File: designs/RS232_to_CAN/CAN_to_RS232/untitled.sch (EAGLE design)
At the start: 22 parts, among them IC1 UART_RS232, IC2 STM32F042K6T6TR, IC3 CAN_Receiver, J1 Programmer, J2 CAN, J3 RS232

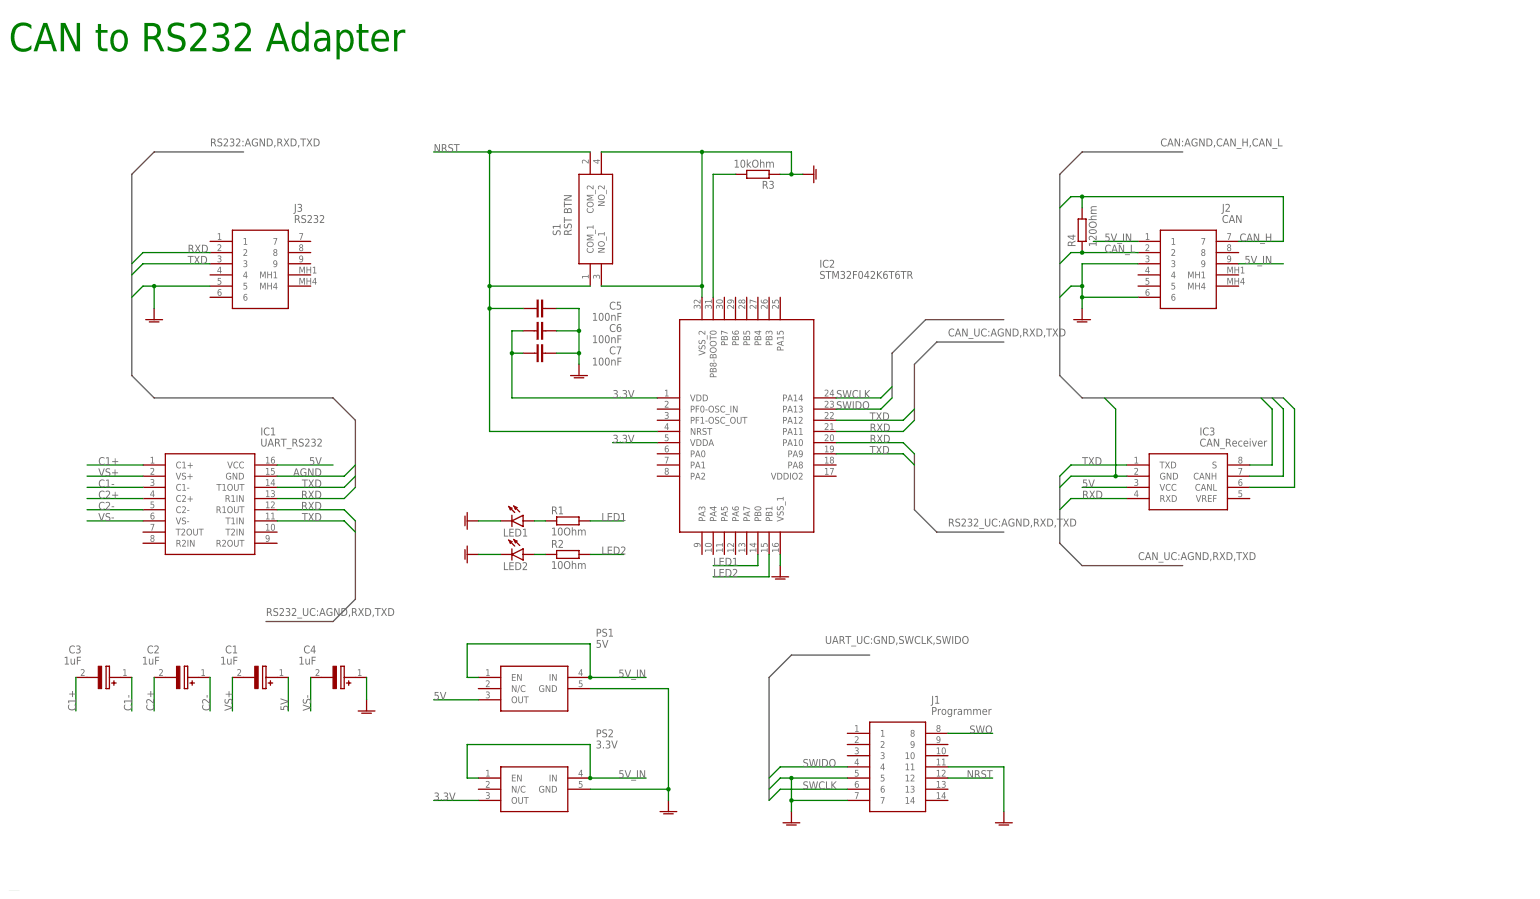
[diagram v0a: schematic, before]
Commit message: ESP32 brd layout
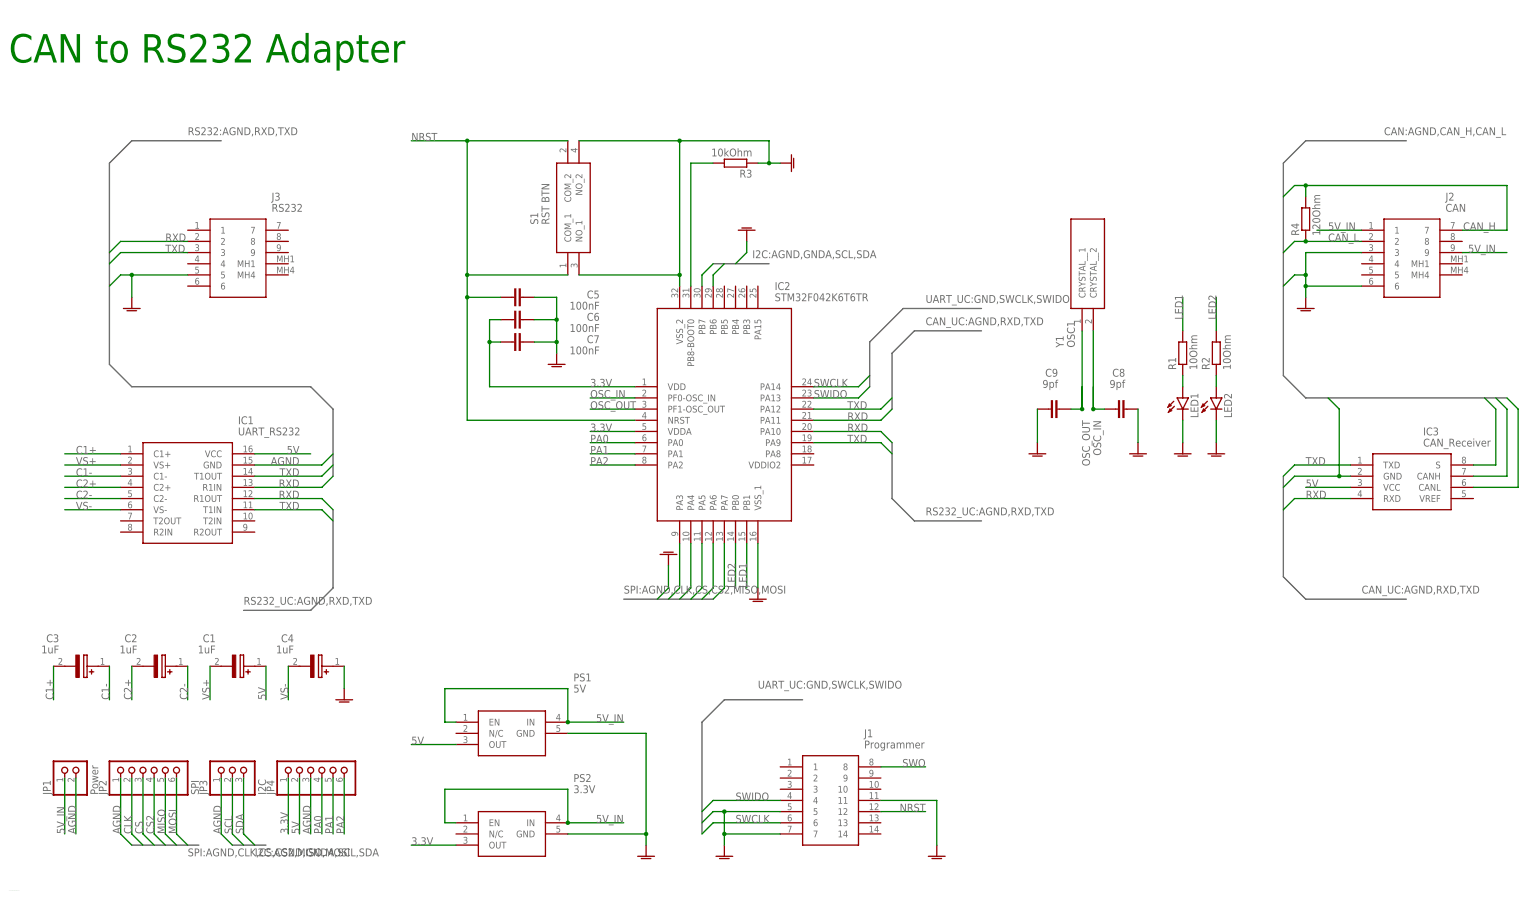
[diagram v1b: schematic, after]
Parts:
- added C8, C9: 9pf, CommonParts:C-EU_805C0805
- added JP1: Power, pinhead:PINHD-1X2/90
- added JP2: SPI, pinhead:PINHD-1X6/90
- added JP3: I2C, pinhead:PINHD-1X3/90
- added JP4: (no value), pinhead:PINHD-1X6/90
- added Y1: OSC1, MouserUseful:CM7V-T1A-32.768KHZ-7PF-100PPM-
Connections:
- removed net N$4: IC2.PB1
- removed net N$5: C2.+
- removed net N$6: C2.-
- removed net N$7: C3.+
- removed net N$8: IC2.PB0
- new net CLK: IC2.PA5, JP2.2
- new net CS: IC2.PA4, JP2.3
- new net CS2: IC2.PA3, JP2.4
- new net MISO: IC2.PA6, JP2.5
- new net MOSI: IC2.PA7, JP2.6
- new net OSC_IN: C8.1, IC2.PF0-OSC_IN, Y1.CRYSTAL__2
- new net OSC_OUT: C9.2, IC2.PF1-OSC_OUT, Y1.CRYSTAL__1
- new net PA0: IC2.PA0, JP4.4
- new net PA1: IC2.PA1, JP4.5
- new net PA2: IC2.PA2, JP4.6
- new net SCL: IC2.PB6, JP3.2
- new net SDA: IC2.PB7, JP3.3
- net 3.3V: now also JP4.1
- net 5V: now also JP4.2
- net 5V_IN: now also JP1.1
- net AGND: now also JP1.2, JP2.1, JP3.1, JP4.3
- net C1-: now also C3.+
- net C2+: now also C2.-
- net C2-: now also C2.+
- net GNDA: now also C8.2, C9.1
- net LED1: now also IC2.PB1
- net LED2: now also IC2.PB0
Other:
- moved on the sheet: C1, C2, C3, C4, C5, C6, C7, IC1, IC2, IC3, J1, J2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

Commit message: added brd layout for RS232 to can
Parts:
- J1: value Programmer -> RS232; device MouserUseful:FTSH-107-01-L-DV-K-A -> MouserUseful:K202XHT-E9S-N
- J2: value CAN -> Programmer; device MouserUseful:K202XHT-E9S-N -> MouserUseful:FTSH-107-01-L-DV-K-A
- J3: value RS232 -> CAN
- JP1: value Power -> (none); device pinhead:PINHD-1X2/90 -> pinhead:PINHD-1X2
- JP2: value SPI -> (none); device pinhead:PINHD-1X6/90 -> pinhead:PINHD-1X6
- JP3: value I2C -> (none); device pinhead:PINHD-1X3/90 -> pinhead:PINHD-1X3
- JP4: device pinhead:PINHD-1X6/90 -> pinhead:PINHD-1X6
- R1: value 10Ohm -> 10kOhm
- R3: value 10kOhm -> 10Ohm
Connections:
- removed net AGND: IC1.GND, IC3.GND, IC3.S, J2.3, J2.6, J3.5, JP1.2, JP2.1, JP3.1, JP4.3
- removed net CAN_H: IC3.CANH, J2.7, R4.2
- removed net CAN_L: IC3.CANL, J2.2, R4.1
- removed net GNDA: C4.+, C5.2, C6.2, C7.2, C8.2, C9.1, IC2.VSS_1, IC2.VSS_2, J1.11, LED1.C, LED2.C, PS1.GND, PS2.GND, R3.1, S1.NO_1, S1.NO_2
- new net CAN_N: IC3.CANL, J3.2, R4.1
- new net CAN_P: IC3.CANH, J3.7, R4.2
- new net CAN_UC_XD_N: IC2.PA11, IC3.RXD
- new net CAN_UC_XD_P: IC2.PA12, IC3.TXD
- new net RXD_UC: IC1.R1OUT, IC2.PA10
- new net TXD_UC: IC1.T1IN, IC2.PA9
- net 3.3V: now also J2.3
- net 5V: now also C3.+; no longer C1.+
- net 5V_IN: now also J3.1, J3.9; no longer J2.1, J2.9
- net C1+: now also C1.-; no longer C3.-
- net C1-: now also C1.+; no longer C3.+
- net CLK: now also JP2.4; no longer JP2.2
- net CS: now also JP2.5; no longer JP2.3
- net CS2: now also JP2.6; no longer JP2.4
- net GND: now also C4.+, C5.2, C6.2, C7.2, C8.1, C9.2, IC1.GND, IC2.VSS_1, IC2.VSS_2, IC3.GND, IC3.S, J2.11, J2.5, J2.7, J3.3, J3.6, JP1.2, JP2.1, JP3.1, JP4.3, LED1.C, LED2.C, PS1.GND, PS2.GND, R1.1, S1.NO_1, S1.NO_2; no longer J1.7
- net LED1: now also R2.2; no longer R1.2
- net LED2: now also R3.2; no longer R2.2
- net MISO: now also JP2.3; no longer JP2.5
- net MOSI: now also JP2.2; no longer JP2.6
- net N$1: now also R2.1; no longer R1.1
- net N$2: now also R3.1; no longer R2.1
- net N$3: now also R1.2; no longer R3.2
- net NRST: now also J2.12; no longer J1.12
- net OSC_IN: now also C9.1; no longer C8.1
- net OSC_OUT: now also C8.2; no longer C9.2
- net RXD: now also J1.2; no longer IC1.R1OUT, IC2.PA10, IC2.PA11, IC3.RXD, J3.2
- net SWCLK: now also J2.6; no longer J1.6
- net SWIDO: now also J2.4; no longer J1.4
- net SWO: now also J2.8; no longer J1.8
- net TXD: now also J1.3; no longer IC1.T1IN, IC2.PA12, IC2.PA9, IC3.TXD, J3.3
- net VS+: now also C3.-; no longer C1.-
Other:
- moved on the sheet: C1, C3, C8, C9, J3, R1, R2, R3

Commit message: added esd for rs232 to can
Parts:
- added D1: PESD2CANFD24V-TR, MouserUseful:PESD2CANFD24V-TR
- added D10: LSM115JE3_TR13, CommonParts:LSM115JE3_TR13
- added D2, D3: SMBJ8.0CA-Q, MouserUseful:SMBJ8.0CA-Q
- added D4, D5, D6, D7, D8, D9: PESD3V3L2BT,215, MouserUseful:PESD3V3L2BT,215
- C1, C2, C3, C4: device CommonParts:UWX1H010MCL2GB -> CommonParts:C-EU_805C0805
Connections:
- net 5V: now also C3.2; no longer C3.+
- net 5V_IN: now also D10.K
- net C1+: now also C1.1; no longer C1.-
- net C1-: now also C1.2; no longer C1.+
- net C2+: now also C2.1; no longer C2.-
- net C2-: now also C2.2; no longer C2.+
- net CAN_N: now also D1.K2
- net CAN_P: now also D1.K1
- net CLK: now also D5.CATHODE_2
- net CS: now also D5.CATHODE_1
- net CS2: now also D6.CATHODE_2
- net GND: now also C4.2, D1.CC, D10.A, D2.1, D3.1, D4.DOUBLE_CATHODE, D5.DOUBLE_CATHODE, D6.DOUBLE_CATHODE, D7.DOUBLE_CATHODE, D8.DOUBLE_CATHODE, D9.DOUBLE_CATHODE; no longer C4.+
- net MISO: now also D4.CATHODE_1
- net MOSI: now also D4.CATHODE_2
- net PA0: now also D8.CATHODE_1
- net PA1: now also D8.CATHODE_2
- net PA2: now also D9.CATHODE_2
- net RXD: now also D3.2
- net SCL: now also D7.CATHODE_1
- net SDA: now also D7.CATHODE_2
- net TXD: now also D2.2
- net VS+: now also C3.1; no longer C3.-
- net VS-: now also C4.1; no longer C4.-
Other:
- note removed: "/Users/moritzbosenberg/Desktop/GIT/EagleParts/designs/OpenHardware.bmp"
- moved on the sheet: C5, C6, C7, C8, C9, IC1, IC2, IC3, J1, J2, J3, JP1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
